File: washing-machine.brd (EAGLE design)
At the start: 112.1 x 90.3 mm, 57 parts, among them IC1 MEGA8-P, IC2 7805TV, K1 ZNS5106, K2 ZNS5106, K3 ZNS5106, Q2 BC547, Q3 BC547, Q4 BC547, Q5 BC547, Q6 BC547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

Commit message: Reroute few wires
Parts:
- turned R13 to 180 degrees
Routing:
- net N$19: track 15.1 -> 4.45 mm
- net GND: track 647.6 -> 657.0 mm
- net N$18: track 6.35 -> 8.89 mm
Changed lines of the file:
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@@
 <attribute name="SPICEMODEL" value="NONE" x="50.8" y="41.91" size="1.778" layer="27" display="off"/>
 </element>
-<element name="R13" library="eagle-ltspice" package="0204/7" value="" x="59.69" y="13.97">
-<attribute name="SPICEPREFIX" value="R" x="59.69" y="13.97" size="1.778" layer="27" display="off"/>
-<attribute name="SPICEMODEL" value="NONE" x="59.69" y="13.97" size="1.778" layer="27" display="off"/>
+<element name="R13" library="eagle-ltspice" package="0204/7" value="" x="59.69" y="13.97" rot="R180">
+<attribute name="SPICEPREFIX" value="R" x="59.69" y="13.97" size="1.778" layer="27" rot="R180" display="off"/>
+<attribute name="SPICEMODEL" value="NONE" x="59.69" y="13.97" size="1.778" layer="27" rot="R180" display="off"/>
 </element>
 <element name="R15" library="eagle-ltspice" package="0204/7" value="" x="58.42" y="45.72" rot="R180">
@@
 <wire x1="60.96" y1="34.29" x2="62.23" y2="34.29" width="0.254" layer="16"/>
 <wire x1="62.23" y1="34.29" x2="66.04" y2="34.29" width="0.5" layer="16"/>
-<wire x1="66.04" y1="18.97" x2="60.96" y2="19.05" width="0.5" layer="16"/>
+<wire x1="66.04" y1="18.97" x2="62.2584" y2="19.033490625" width="0.5" layer="16"/>
+<wire x1="62.2584" y1="19.033490625" x2="60.96" y2="19.05" width="0.5" layer="16"/>
 <wire x1="66.04" y1="11.43" x2="66.04" y2="18.97" width="0.5" layer="16"/>
 <wire x1="62.23" y1="24.63" x2="62.23" y2="34.29" width="0.5" layer="16"/>
@@
 <wire x1="37.1" y1="1.54" x2="4.16" y2="1.54" width="0.5" layer="16"/>
 <wire x1="39.37" y1="3.81" x2="37.1" y2="1.54" width="0.5" layer="16"/>
-<wire x1="66.04" y1="10.16" x2="66.04" y2="11.43" width="0.254" layer="16"/>
-<wire x1="65.7225" y1="10.16" x2="66.04" y2="10.16" width="0.254" layer="16"/>
-<wire x1="64.77" y1="9.2075" x2="65.7225" y2="10.16" width="0.254" layer="16"/>
-<wire x1="64.77" y1="6.215" x2="64.77" y2="9.2075" width="0.254" layer="16"/>
-<wire x1="79.7875" y1="6.215" x2="64.77" y2="6.215" width="0.5" layer="16"/>
+<wire x1="79.7875" y1="6.215" x2="62.2584" y2="6.215" width="0.5" layer="16"/>
 <wire x1="81.51" y1="3.4925" x2="79.7875" y2="6.215" width="0.5" layer="16"/>
 <wire x1="81.51" y1="0.77" x2="81.51" y2="3.4925" width="0.5" layer="16"/>
@@
 <wire x1="2.54" y1="73.215" x2="1.27" y2="73.215" width="0.5" layer="16"/>
 <wire x1="103.755" y1="78.74" x2="103.755" y2="71.12" width="0.5" layer="16"/>
+<wire x1="62.2584" y1="6.215" x2="62.2584" y2="19.033490625" width="0.5" layer="16"/>
 </signal>
 <signal name="+12V">
@@
 <contactref element="Q3" pad="B"/>
 <contactref element="R13" pad="1"/>
-<wire x1="57.15" y1="15.24" x2="55.88" y2="13.97" width="0.5" layer="16"/>
-<wire x1="65.0675" y1="15.24" x2="57.15" y2="15.24" width="0.5" layer="16"/>
-<wire x1="65.02" y1="12.7875" x2="65.0675" y2="15.24" width="0.5" layer="16"/>
-<wire x1="64.27" y1="12.16" x2="65.02" y2="12.7875" width="0.5" layer="16"/>
-<wire x1="64.135" y1="10.16" x2="64.27" y2="12.16" width="0.5" layer="16"/>
+<wire x1="63.5" y1="13.97" x2="64.135" y2="13.97" width="0.4064" layer="16"/>
+<wire x1="64.135" y1="13.97" x2="64.135" y2="10.16" width="0.5" layer="16"/>
 </signal>
 <signal name="N$18">
 <contactref element="R13" pad="2"/>
 <contactref element="OK2" pad="3"/>
-<wire x1="60.96" y1="13.97" x2="60.96" y2="10.16" width="0.5" layer="16"/>
-<wire x1="63.5" y1="13.97" x2="60.96" y2="13.97" width="0.5" layer="16"/>
+<wire x1="55.88" y1="13.97" x2="60.96" y2="13.97" width="0.4064" layer="16"/>
+<wire x1="60.96" y1="13.97" x2="60.96" y2="10.16" width="0.4064" layer="16"/>
 </signal>
 <signal name="DRAINRELAY">

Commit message: Minor modifications in the layout
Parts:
- added JP7: (no value), pinhead:1X01
- added JP8: (no value), pinhead:1X02
- JP2: device pinhead:1X02 -> pinhead:1X03
- moved JP2 5.64 mm to (10.1, 80.9)
- moved IC2 3.50 mm to (10.2, 79.0)
- turned C2 to 90 degrees
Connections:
- new net N$31: IC1.3, JP8.2
- new net N$38: IC1.2, JP8.1
- new net N$39: IC1.24, JP7.1
- net +5V: now also JP2.3
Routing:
- net GND: track 657.0 -> 0.22 mm
- net SELECTBUTTON: track 78.4 -> 83.8 mm
- net UPBUTTON: track 71.4 -> 76.7 mm
- net +5V: track 290.4 -> 295.0 mm
- net N$31: track 0.00 -> 3.35 mm
- net N$38: track 0.00 -> 3.31 mm
- net N$39: track 0.00 -> 3.29 mm
- net RESET: track 161.0 -> 164.0 mm
- net DOWNBUTTON: track 92.3 -> 94.2 mm
- added copper zone on layer 16, net GND

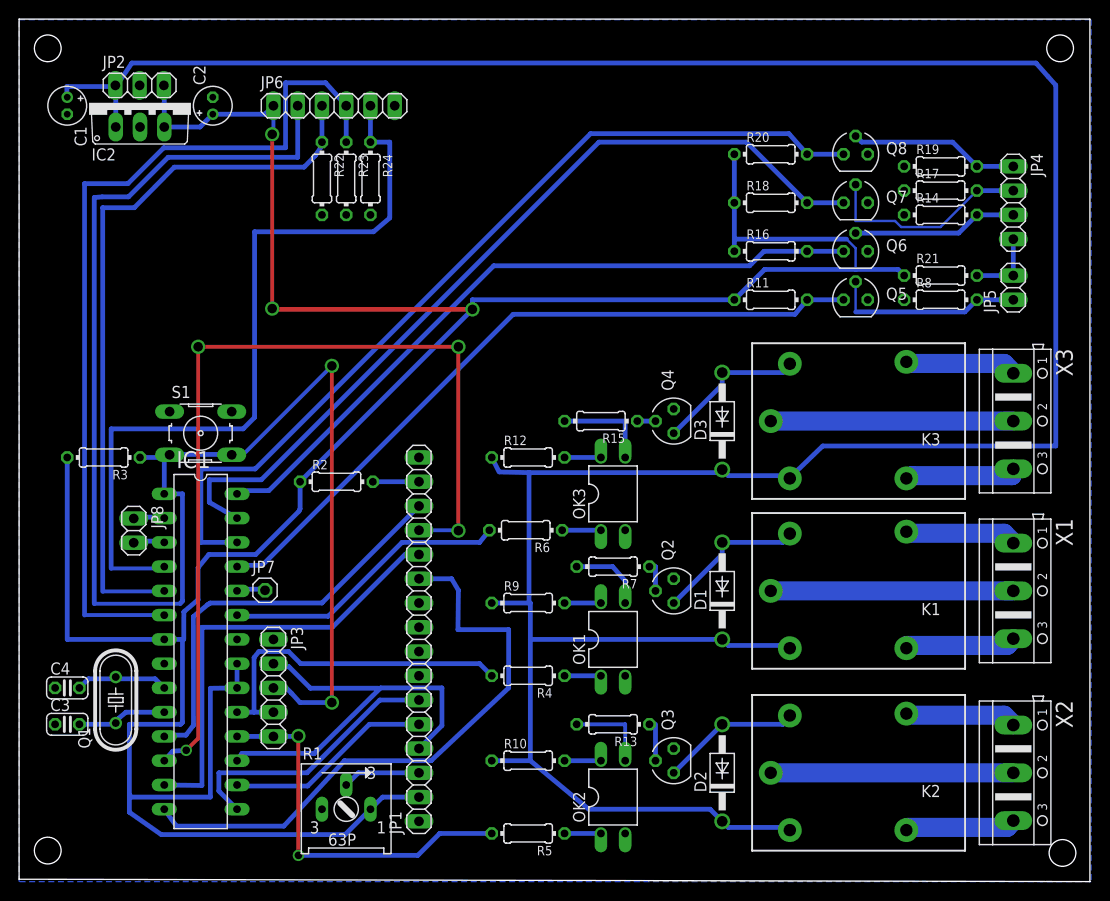
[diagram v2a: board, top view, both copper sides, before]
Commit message: Change layout to increase ground plane
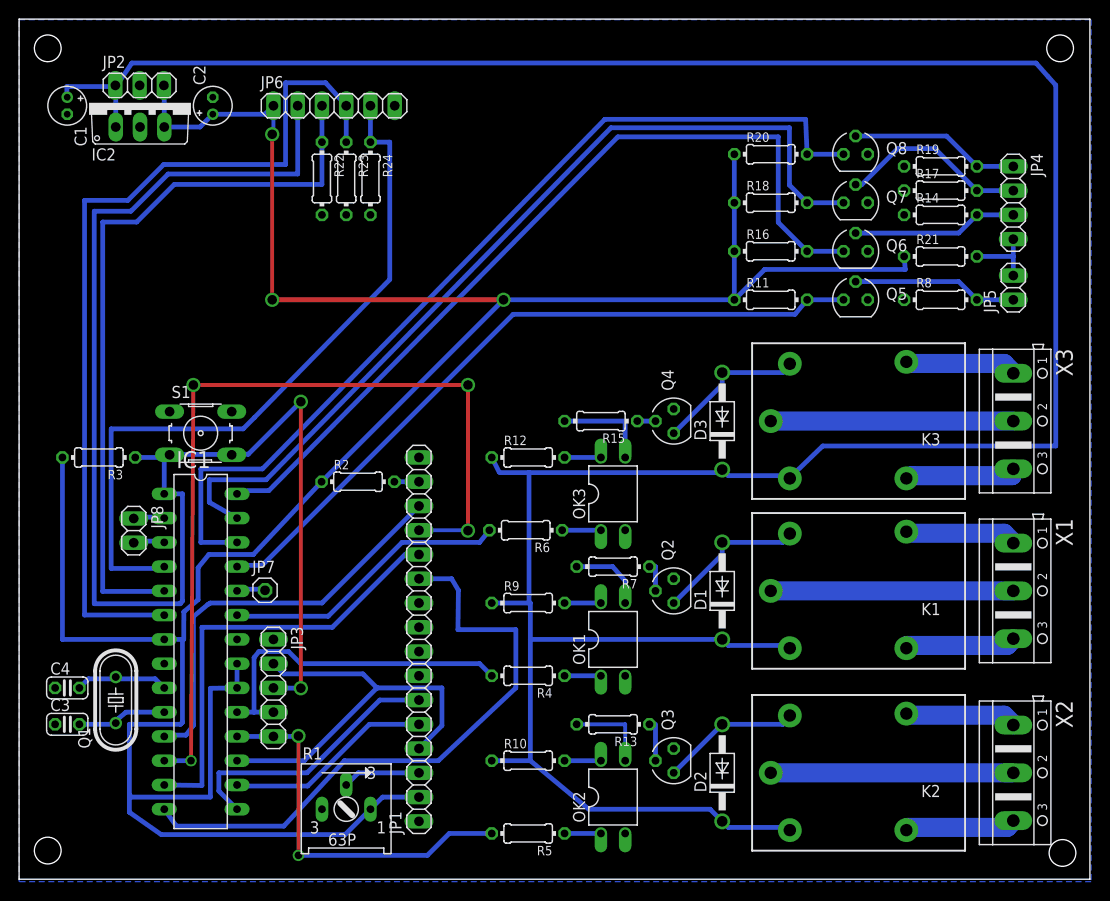
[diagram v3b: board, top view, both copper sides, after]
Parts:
- moved R2 2.25 mm to (33.0, 39.4)
- moved R21 2.00 mm to (94.0, 63.0)
- moved R3 0.50 mm to (5.85, 41.9)
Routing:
- net LOWSENSOR: track 74.1 -> 89.5 mm
- net RESET: track 164.0 -> 150.8 mm
- net +5V: track 295.0 -> 286.6 mm
- net SELECTBUTTON: track 83.8 -> 76.3 mm
- net MIDSENSOR: track 89.4 -> 94.4 mm
- net N$3: track 96.2 -> 91.3 mm
- net HIGHSENSOR: track 94.3 -> 97.7 mm
- net DSPIN: track 20.2 -> 17.3 mm
- net MSPIN: track 22.2 -> 19.9 mm
- net N$28: track 4.83 -> 2.58 mm
- net N$7: track 63.3 -> 64.8 mm
- net UPBUTTON: track 76.7 -> 78.0 mm
- net N$4: track 44.4 -> 43.9 mm
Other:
- board size 112.1 x 90.3 mm -> 112.1 x 90.1 mm

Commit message: Remove ground plane to ease of circuit printing
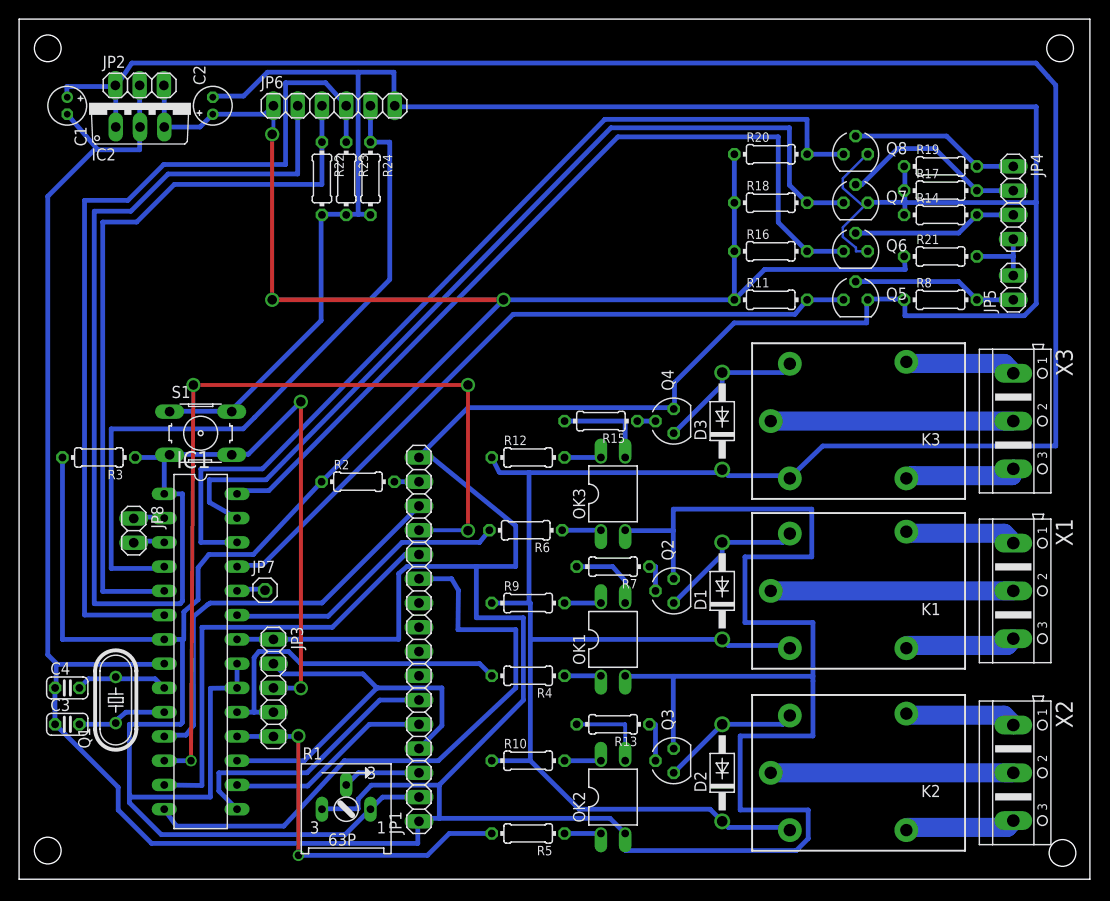
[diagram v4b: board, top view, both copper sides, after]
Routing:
- net GND: track 0.22 -> 681.5 mm
- removed copper zone on layer 16, net GND
